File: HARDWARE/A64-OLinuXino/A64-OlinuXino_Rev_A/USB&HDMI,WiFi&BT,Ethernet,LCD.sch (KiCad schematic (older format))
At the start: 117 parts, among them Q1 E4SB25.000F20E15(25MHz/20pF/2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, U1 AllWinner-A64(FBGA396), U10 RTL8211CL-GR(LQFP48), U11 SY6280AAC(SOT23-5), U12 SY6280AAC(SOT23-5), U6 RTL8723BS(ComboModule), U7 NA(RCLAMP0524P), U8 NA(RCLAMP0524P), U9 NA(RCLAMP0524P)

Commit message: A64-OLinuXino component placement, all components libraries updated
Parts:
- removed LCD_CON1: GBH-254-SMT-40, symbol ML40YA-V36P-2X20-LF
- added C196: 100nF, OLIMEX_RLC-FP:C_0402_5MIL_DWS, symbol C
- added LCD_CON1: FPV-WZA21-40-LF, OLIMEX_Connectors-FP:FPV-WZA21-40-LF, symbol LCD-ML40YA-V36P-2X20-LF
- added R100, R99: NA(2.2k), OLIMEX_RLC-FP:R_0402_5MIL_DWS, symbol R
- added U15: AT24C16BN-SH(SO-8_150mil), OLIMEX_IC-FP:SO-8, symbol AT24C16BN-SH(SO-8_150mil)
- ANT1: value WIFI_ANT_ESP8266??? -> PCB_WIFI_ANT; footprint (none) -> OLIMEX_Antennas-FP:bt_antenna_1ant_2gnd
- FET1: footprint (none) -> OLIMEX_Transistors-FP:SOT23
- FUSE1: footprint (none) -> OLIMEX_Devices-FP:FUSE-1206
- HDMI1: footprint (none) -> OLIMEX_Connectors-FP:HDMI-SWM-19
- L10: renamed from L6; footprint (none) -> OLIMEX_RLC-FP:L_0805_5MIL_DWS
- L11: renamed from L7; footprint (none) -> OLIMEX_RLC-FP:L_0805_5MIL_DWS
- L12: renamed from L8; footprint (none) -> OLIMEX_RLC-FP:L_0805_5MIL_DWS
- L13: renamed from L9; footprint (none) -> OLIMEX_RLC-FP:CD42(43)
- L6: renamed from L10; footprint (none) -> OLIMEX_RLC-FP:L_0805_5MIL_DWS
- L7: renamed from L12; footprint (none) -> OLIMEX_RLC-FP:L_0805_5MIL_DWS
- L8: renamed from L11; footprint (none) -> OLIMEX_RLC-FP:L_0805_5MIL_DWS
- L9: renamed from L13; footprint (none) -> OLIMEX_RLC-FP:L_0805_5MIL_DWS
- LAN1: footprint (none) -> OLIMEX_Connectors-FP:TM211Q01FM22
- PHYRST1: footprint (none) -> OLIMEX_Jumpers-FP:HN1x2_Jumper
- Q1: footprint (none) -> OLIMEX_Crystal-FP:Q5x3.25
- R37: renamed from R72; footprint OLIMEX_RLC-FP:R_0603_5MIL_DWS -> OLIMEX_RLC-FP:R_0402_5MIL_DWS
- R38: renamed from R71; footprint OLIMEX_RLC-FP:R_0603_5MIL_DWS -> OLIMEX_RLC-FP:R_0402_5MIL_DWS
- R40: renamed from R65; footprint OLIMEX_RLC-FP:R_0603_5MIL_DWS -> OLIMEX_RLC-FP:R_0402_5MIL_DWS
- R41: renamed from R68; footprint OLIMEX_RLC-FP:R_0603_5MIL_DWS -> OLIMEX_RLC-FP:R_0402_5MIL_DWS
- R42: renamed from R69; footprint OLIMEX_RLC-FP:R_0603_5MIL_DWS -> OLIMEX_RLC-FP:R_0402_5MIL_DWS
- R49: renamed from R70; value 13k/1% -> 3.92k/1%
- R61: renamed from R44; footprint OLIMEX_RLC-FP:R_0603_5MIL_DWS -> OLIMEX_RLC-FP:R_0402_5MIL_DWS
- R67: renamed from R55; value NA -> 1k
- RM10: renamed from RM11; footprint (none) -> OLIMEX_RLC-FP:RA0805_(4X0402)_xx
- RM11: renamed from RM12; footprint (none) -> OLIMEX_RLC-FP:RA0805_(4X0402)_xx
- RM12: renamed from RM10; footprint (none) -> OLIMEX_RLC-FP:RA1206_(4X0603)_4B8_xx
- RM13: footprint (none) -> OLIMEX_RLC-FP:RA0805_(4X0402)_xx
- RM9: footprint (none) -> OLIMEX_RLC-FP:RA1206_(4X0603)_4B8_xx
- TP1: footprint (none) -> OLIMEX_Other-FP:TESTPAD_40-ROUND
- U1: footprint (none) -> OLIMEX_IC-FP:FBGA396
- U10: renamed from U9; value NA(RCLAMP0524P) -> NA(RCLAMP0524P(SLP2510P8)); footprint (none) -> OLIMEX_Devices-FP:SLP2510P8
- U11: renamed from U6; footprint (none) -> OLIMEX_IC-FP:RL-SM02BD(RTL8723BS)
- U12: renamed from U10; footprint (none) -> OLIMEX_IC-FP:LQFP48
- U6: renamed from U11; footprint (none) -> OLIMEX_IC-FP:SOT-23-5
- U7, U8: value NA(RCLAMP0524P) -> NA(RCLAMP0524P(SLP2510P8)); footprint (none) -> OLIMEX_Devices-FP:SLP2510P8
- U9: renamed from U12; footprint (none) -> OLIMEX_IC-FP:SOT-23-5
- USB-OTG1: value MICRO_USB/A01SB141B1-261 -> MICRO_USB/MISB-SWMM-5AB_LF; footprint (none) -> OLIMEX_Connectors-FP:USB-MICRO-5P-F
- USB1: footprint (none) -> OLIMEX_Connectors-FP:USB_PN87520_HOST_PTH
- renumbered C91 to C100, C92 to C101, C93 to C102, C94 to C103, C95 to C104, C72 to C105, C73 to C106, C74 to C107, C96 to C108, C71 to C109, C75 to C110, C98 to C111, C99 to C112, C100 to C113, C101 to C114, C111 to C67, C107 to C68, C109 to C69, C113 to C70, C103 to C71, C106 to C72, C97 to C73, C112 to C74, C108 to C75, C110 to C76, C114 to C77, C104 to C78, C76 to C79, C105 to C80, C77 to C81, C78 to C82, C79 to C83, C80 to C84, C81 to C85, C82 to C86, C83 to C87, C102 to C88, C67 to C89, C68 to C90, C69 to C91, C70 to C92, C84 to C93, C85 to C94, C86 to C95, C87 to C96, C88 to C97, C89 to C98, C90 to C99, R46 to R39, R47 to R43, R48 to R44, R49 to R45, R41 to R46, R37 to R47, R67 to R48, R38 to R50, R39 to R51, R40 to R52, R62 to R53, R43 to R54, R52 to R55, R50 to R56, R63 to R57, R64 to R58, R51 to R59, R42 to R60, R45 to R62, R53 to R63, R60 to R64, R61 to R65, R54 to R66, R56 to R68, R57 to R69, R66 to R70, R73 to R71, R58 to R72, R59 to R73
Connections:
- net VBAT-EXT is gone; now on net +3V3: C89.2, C90.2, U11.9 (VDD33)
- net +3.3VWiFiIO: now also RM12.2.1
- net +3V3: now also C196.2, LCD_CON1.3, R100.1, R99.2, U15.8 (VCC)
- net +5V: now also LCD_CON1.1
- net BT-RST-N: now also RM12.4.2; no longer RM12.3.2
- net BT-UART-RX: now also RM12.3.2; no longer RM12.4.2
- net GMDC/LCD-PWM: now also LCD_CON1.36
- net GMDIO/LCD_PWR: now also LCD_CON1.35
- net GND: now also C196.1, LCD_CON1.13, LCD_CON1.14, LCD_CON1.2, LCD_CON1.21, LCD_CON1.22, LCD_CON1.4, LCD_CON1.5, LCD_CON1.6, U15.1 (A0), U15.2 (A1), U15.3 (A2), U15.4 (GND), U15.7 (WP); no longer RM12.2.1
- net GRXCK/LCD_D18: now also LCD_CON1.7
- net GRXCTL/LCD_D19: now also LCD_CON1.8
- net GRXD0/LCD_D15: now also LCD_CON1.20
- net GRXD1/LCD_D14: now also LCD_CON1.19
- net GRXD2/LCD_D13: now also LCD_CON1.18
- net GRXD3/LCD_D12: now also LCD_CON1.17
- net GTXCK/LCD_DE: now also LCD_CON1.32
- net GTXCTL/LCD_HSYNC: now also LCD_CON1.29
- net GTXD0/LCD_CLK: now also LCD_CON1.31
- net GTXD1/LCD_D23: now also LCD_CON1.12
- net GTXD2/LCD_D22: now also LCD_CON1.11
- net GTXD3/LCD_D21: now also LCD_CON1.10
- net LCD_D10: now also LCD_CON1.15
- net LCD_D11: now also LCD_CON1.16
- net LCD_D2: now also LCD_CON1.23
- net LCD_D20: now also LCD_CON1.9
- net LCD_D3: now also LCD_CON1.24
- net LCD_D4: now also LCD_CON1.25
- net LCD_D5: now also LCD_CON1.26
- net LCD_D6: now also LCD_CON1.27
- net LCD_D7: now also LCD_CON1.28
- net PH10: now also LCD_CON1.33
- net PH11: now also LCD_CON1.34
- net PH7/CTP-INT: now also LCD_CON1.37
- net PH8/CTP-RST: now also LCD_CON1.38
- net TWI0-SCK: now also LCD_CON1.39, R100.2, U15.6 (SCL)
- net TWI0-SDA: now also LCD_CON1.40, R99.1, U15.5 (SDA)
- net WL-PMU-EN: now also RM12.1.2; no longer RM12.2.2
- net WL-SDIO-CMD: now also RM12.2.2; no longer RM12.1.2
- net WL-SDIO-D0: now also RM9.3.2; no longer RM9.4.2
- net WL-SDIO-D1: now also RM9.4.2; no longer RM9.3.2
- net WL-SDIO-D2: now also RM9.1.2; no longer RM9.2.2
- net WL-SDIO-D3: now also RM9.2.2; no longer RM9.1.2
- net CLK125/LCD_VSYNC renamed GCLKIN/LCD_VSYNC
- net GCLKIN/LCD_VSYNC: now also LCD_CON1.30
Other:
- note added: "After testing to be specified if R58 will remain NA or 22R! Gogo will say!"
- note added: "Ilim(A)=6800/Rset(Ohm)"
- note added: "Ilim=0.5A"
- note added: "Ilim=1.7A"
- note added: "MAC Address Option\n==================\nEEPROM - 16 Kbit(2048 x 8)\nI2C Address: 0x50"
- note added: "Rset"
- note added: "WL_DSI# is pulled up because VCC-PL is 1.8V"
- note removed: "The schematic was checked\nfrom Root up to Here!!!!!"
- moved on the sheet: C74, C75, C76, C77, C78, L8, L9, R48, R49, RM12B, RM12C, RM12D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

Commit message: A64-OLinuXino update
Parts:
- removed C196: 100nF, OLIMEX_RLC-FP:C_0402_5MIL_DWS, symbol C
- removed R100, R99: NA(2.2k), OLIMEX_RLC-FP:R_0402_5MIL_DWS, symbol R
- removed U15: AT24C16BN-SH(SO-8_150mil), OLIMEX_IC-FP:SO-8, symbol AT24C16BN-SH(SO-8_150mil)
- R46, R47, R48, R49, R50, R51, R52, R53, R55, R56, R57, R58, R59, R63, R64, R65, R66, R67, R68, R69, R70, R71, R72, R73: footprint OLIMEX_RLC-FP:R_0603_5MIL_DWS -> OLIMEX_RLC-FP:R_0402_5MIL_DWS
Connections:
- net GRXCK/LCD_D18: now also RM13.1.2; no longer RM13.2.2
- net GRXCTL/LCD_D19: now also RM13.2.2; no longer RM13.1.2
- net GRXD0/LCD_D15: now also RM11.2.2; no longer RM11.1.2
- net GRXD1/LCD_D14: now also RM11.3.2; no longer RM11.2.2
- net GRXD2/LCD_D13: now also RM11.1.2; no longer RM11.3.2
- net at RM11.1.1: now also RM10.2.1, U12.17 (RXD[2]/AN0); no longer U12.14 (RXD[0])
- net at R53.2, U12.16 (RXD[1]/TXDLY): now also RM10.3.1, RM11.3.1; no longer RM10.1.1, RM11.2.1
- net at RM11.4.1, U12.18 (RXD[3]/AN1): now also RM10.1.1; no longer RM10.3.1
- net at RM10.4.1, U12.13 (RXCTL/RXDV): now also RM13.2.1; no longer RM13.1.1
- net at C88.2, U12.19 (RXC): now also RM13.1.1; no longer RM13.2.1
- new net: RM11.2.1, U12.14 (RXD[0])
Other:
- note removed: "MAC Address Option\n==================\nEEPROM - 16 Kbit(2048 x 8)\nI2C Address: 0x50"
- note removed: "WL_DSI# is pulled up because VCC-PL is 1.8V"
- moved on the sheet: RM10A, RM10C, RM11A, RM11B, RM11C, RM13A, RM13B

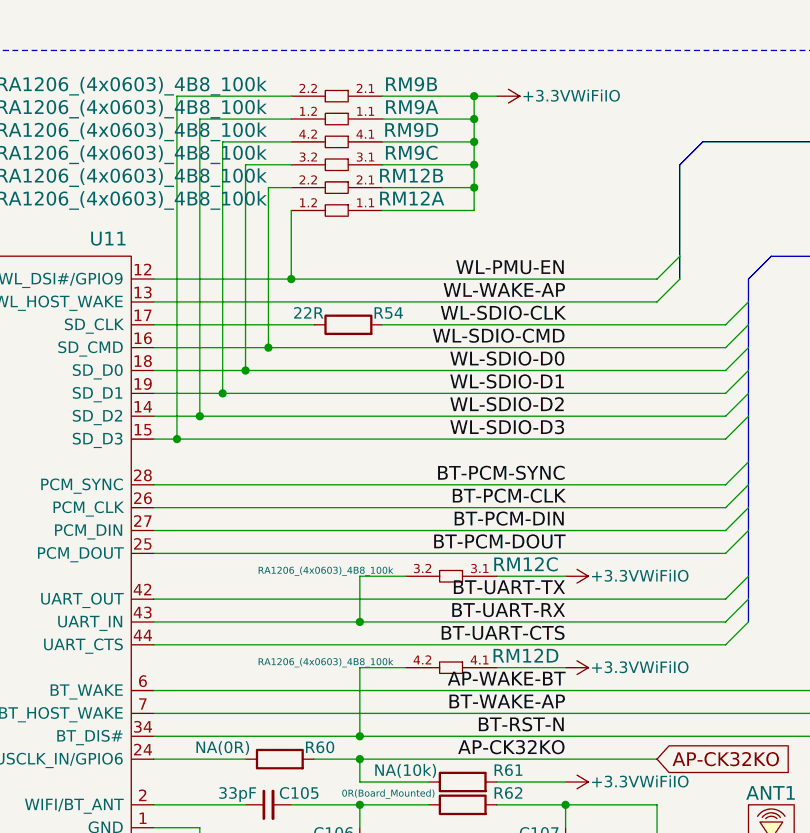
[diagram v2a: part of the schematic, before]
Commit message: A64-OLinuXino routing completed
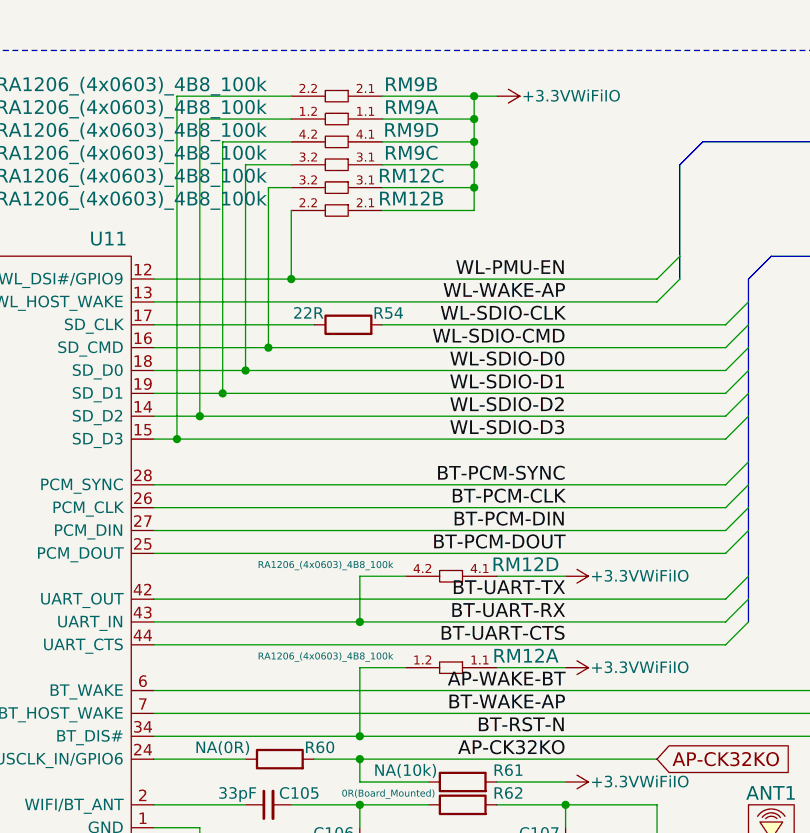
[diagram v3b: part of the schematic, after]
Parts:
- USB-OTG1: footprint OLIMEX_Connectors-FP:USB-MICRO-5P-F -> OLIMEX_Connectors-FP:USB-MICRO_MISB-SWMM-5B_LF
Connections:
- net BT-RST-N: now also RM12.1.2; no longer RM12.4.2
- net BT-UART-RX: now also RM12.4.2; no longer RM12.3.2
- net WL-PMU-EN: now also RM12.2.2; no longer RM12.1.2
- net WL-SDIO-CMD: now also RM12.3.2; no longer RM12.2.2
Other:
- moved on the sheet: RM12A, RM12B, RM12C, RM12D
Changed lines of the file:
@@
 EESchema Schematic File Version 2
+LIBS:OLIMEX_Antennas
+LIBS:OLIMEX_Buttons
+LIBS:OLIMEX_Connectors
+LIBS:OLIMEX_Devices
+LIBS:OLIMEX_Diodes
+LIBS:OLIMEX_IC
+LIBS:OLIMEX_Jumpers
+LIBS:OLIMEX_OTHER
+LIBS:OLIMEX_Power
+LIBS:OLIMEX_RCL
+LIBS:OLIMEX_Regulators
+LIBS:OLIMEX_Switches
+LIBS:OLIMEX_Transistors
 LIBS:A64-OlinuXino_Rev_A-cache
 EELAYER 25 0
@@
 F 0 "USB-OTG1" H 15500 1800 50  0000 C CNN
 F 1 "MICRO_USB/MISB-SWMM-5AB_LF" H 15200 1100 35  0000 C CNN
-F 2 "OLIMEX_Connectors-FP:USB-MICRO-5P-F" H 15700 1400 60  0001 C CNN
+F 2 "OLIMEX_Connectors-FP:USB-MICRO_MISB-SWMM-5B_LF" H 15700 1400 60  0001 C CNN
 F 3 "" H 15700 1400 60  0000 C CNN
 	1    15700 1400
@@
 L RA1206_(4x0603)_4B8_Smashed RM12
 U 1 1 563630D6
+P 4100 6850
+F 0 "RM12" H 3775 7050 60  0000 C CNN
+F 1 "RA1206_(4x0603)_4B8_100k" H 4650 7050 30  0000 C CNN
+F 2 "OLIMEX_RLC-FP:RA1206_(4X0603)_4B8_xx" H 4150 6750 60  0001 C CNN
+F 3 "" H 4150 6750 60  0000 C CNN
+	1    4100 6850
+	-1   0    0    -1
+$EndComp
+$Comp
+L RA1206_(4x0603)_4B8_Smashed RM12
+U 2 1 563632B1
 P 3600 4850
 F 0 "RM12" H 3275 5050 60  0000 C CNN
@@
 F 2 "OLIMEX_RLC-FP:RA1206_(4X0603)_4B8_xx" H 3650 4750 60  0001 C CNN
 F 3 "" H 3650 4750 60  0000 C CNN
-	1    3600 4850
+	2    3600 4850
 	-1   0    0    -1
 $EndComp
 $Comp
 L RA1206_(4x0603)_4B8_Smashed RM12
-U 2 1 563632B1
+U 3 1 56363565
 P 3600 4750
 F 0 "RM12" H 3275 4950 60  0000 C CNN
@@
 F 2 "OLIMEX_RLC-FP:RA1206_(4X0603)_4B8_xx" H 3650 4650 60  0001 C CNN
 F 3 "" H 3650 4650 60  0000 C CNN
-	2    3600 4750
-	-1   0    0    -1
-$EndComp
-$Comp
-L RA1206_(4x0603)_4B8_Smashed RM12
-U 3 1 56363565
-P 4100 6450
-F 0 "RM12" H 3775 6650 60  0000 C CNN
-F 1 "RA1206_(4x0603)_4B8_100k" H 4650 6625 30  0000 C CNN
-F 2 "OLIMEX_RLC-FP:RA1206_(4X0603)_4B8_xx" H 4150 6350 60  0001 C CNN
-F 3 "" H 4150 6350 60  0000 C CNN
-	3    4100 6450
+	3    3600 4750
 	-1   0    0    -1
 $EndComp
@@
 L RA1206_(4x0603)_4B8_Smashed RM12
 U 4 1 56301F8A
-P 4100 6850
-F 0 "RM12" H 3775 7050 60  0000 C CNN
-F 1 "RA1206_(4x0603)_4B8_100k" H 4650 7025 30  0000 C CNN
-F 2 "OLIMEX_RLC-FP:RA1206_(4X0603)_4B8_xx" H 4150 6750 60  0001 C CNN
-F 3 "" H 4150 6750 60  0000 C CNN
-	4    4100 6850
-	-1   0    0    -1
-$EndComp
+P 4100 6450
+F 0 "RM12" H 3775 6650 60  0000 C CNN
+F 1 "RA1206_(4x0603)_4B8_100k" H 4650 6650 30  0000 C CNN
+F 2 "OLIMEX_RLC-FP:RA1206_(4X0603)_4B8_xx" H 4150 6350 60  0001 C CNN
+F 3 "" H 4150 6350 60  0000 C CNN
+	4    4100 6450
+	-1   0    0    -1
+$EndComp
